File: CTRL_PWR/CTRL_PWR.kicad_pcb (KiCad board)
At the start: 2 copper layers, 34 x 17 mm, 9 parts, among them J1 BM09B-NSHSS-TBT_LF__SN_

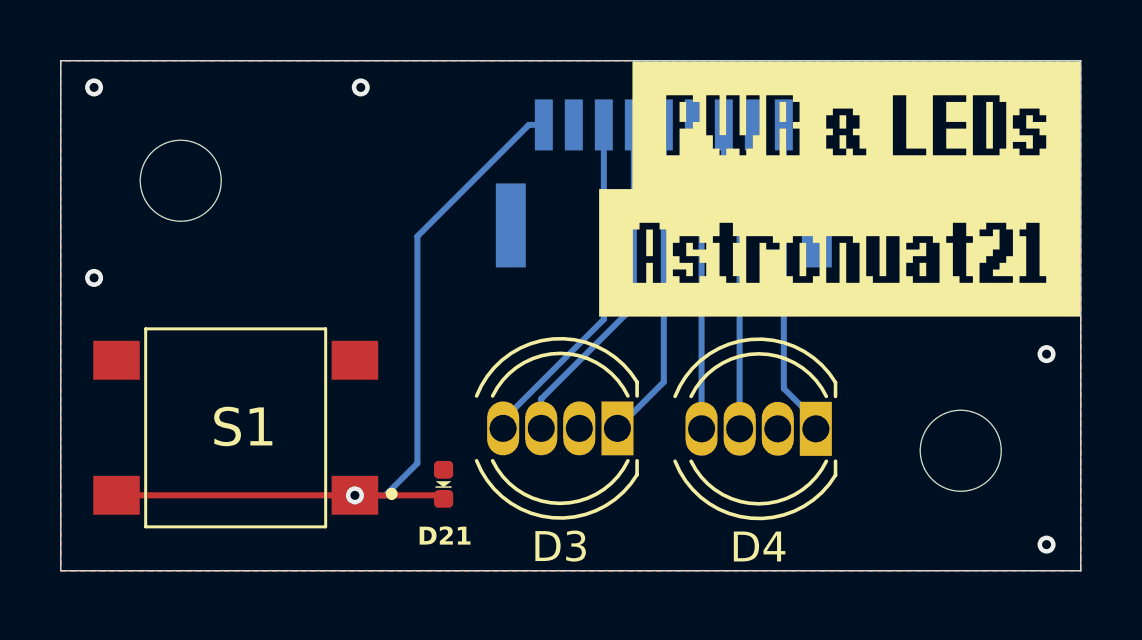
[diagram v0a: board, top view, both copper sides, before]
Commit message: CTRL_PWR updated to use 8P FPC Connector
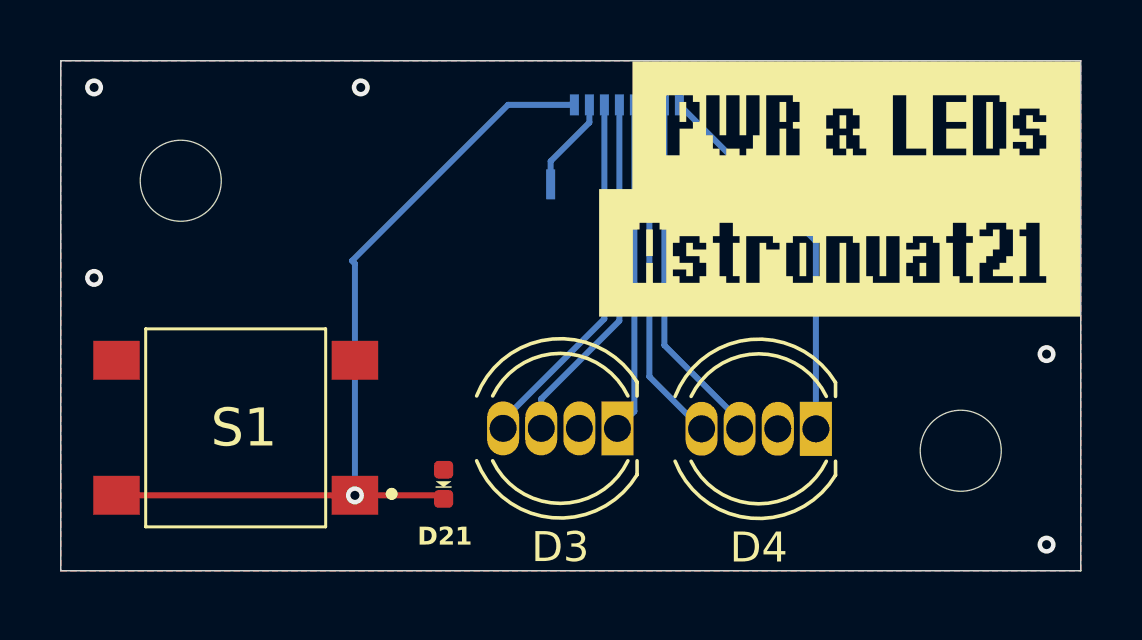
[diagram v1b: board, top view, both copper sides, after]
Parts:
- removed J1: BM09B-NSHSS-TBT_LF__SN_, BM09B-NSHSS-TBT_LF__SN_:BM09BNSHSSTBTLFSN
- added J2: 503480-0800, 503480-0800:5034800800, B.Cu at (94.0, 105.0)
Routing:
- net GND: track 0.00 -> 3.18 mm
- net Net-(D4-RA): track 10.6 -> 12.7 mm
- net Net-(D21-A1): track 26.8 -> 28.4 mm
- net Net-(D4-GA): track 10.3 -> 11.8 mm
- net Net-(D4-BA): track 10.4 -> 11.5 mm
- net Net-(D3-BA): track 11.5 -> 12.2 mm

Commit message: Updated CTRL_Z to use 3 pin FPC and ESD Protection.
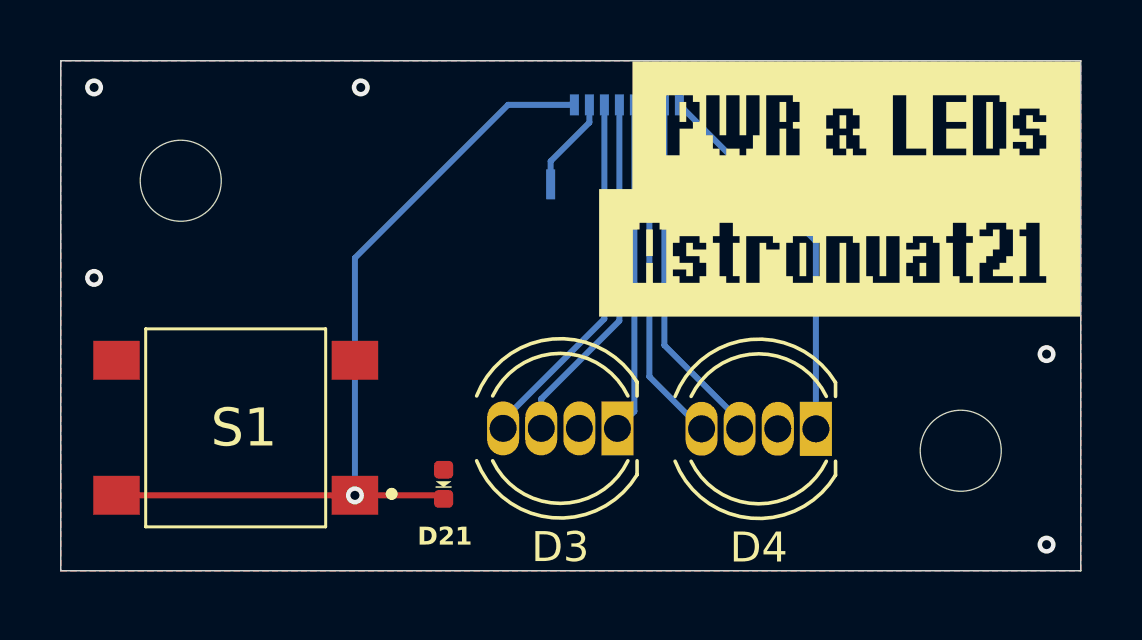
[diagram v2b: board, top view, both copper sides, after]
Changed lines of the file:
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@@
 	)
 	(segment
-		(start 84.8 108.65)
-		(end 84.895 108.745)
+		(start 92.21 103.45)
+		(end 90 103.45)
+		(width 0.2)
+		(layer "B.Cu")
+		(net "Net-(D21-A1)")
+	)
+	(segment
+		(start 84.895 108.555)
+		(end 84.895 116.468)
 		(width 0.2)
 		(layer "B.Cu")
@@
 	(segment
 		(start 90 103.45)
-		(end 84.8 108.65)
+		(end 84.895 108.555)
 		(width 0.2)
 		(layer "B.Cu")
-		(net "Net-(D21-A1)")
-	)
-	(segment
-		(start 84.895 108.745)
-		(end 84.895 116.468)
-		(width 0.2)
-		(layer "B.Cu")
-		(net "Net-(D21-A1)")
-	)
-	(segment
-		(start 92.21 103.45)
-		(end 90 103.45)
-		(width 0.2)
-		(layer "B.Cu")

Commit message: Added resistors to the LEDs on CTRL_PWR
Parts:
- removed kibuzzard-6A2CAA19: G***, kibuzzard-6A2CAA19
- added R1: 180R, Resistor_SMD:R_0402_1005Metric, B.Cu at (93.7, 110.0)
- added R2: 180R, Resistor_SMD:R_0402_1005Metric, B.Cu at (100.2, 110.0)
- added R3: 47R, Resistor_SMD:R_0402_1005Metric, B.Cu at (91.1, 109.9)
- added R4: 47R, Resistor_SMD:R_0402_1005Metric, B.Cu at (89.8, 110.0)
- added R5: 47R, Resistor_SMD:R_0402_1005Metric, B.Cu at (97.7, 109.9)
- added R6: 47R, Resistor_SMD:R_0402_1005Metric, B.Cu at (96.5, 110.0)
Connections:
- J2 pad 1: Net-(D4-RA) -> Net-(J2-Pad1)
- J2 pad 2: Net-(D4-GA) -> Net-(J2-Pad2)
- J2 pad 3: Net-(D4-BA) -> Net-(J2-Pad3)
- J2 pad 4: Net-(D3-RA) -> Net-(J2-Pad4)
- J2 pad 5: Net-(D3-GA) -> Net-(J2-Pad5)
- J2 pad 6: Net-(D3-BA) -> Net-(J2-Pad6)
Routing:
- net Net-(D4-RA): track 12.7 -> 3.79 mm
- net Net-(D3-BA): track 12.2 -> 3.74 mm
- net Net-(D3-GA): track 11.9 -> 3.79 mm
- net Net-(D4-GA): track 11.8 -> 3.81 mm
- net Net-(J2-Pad1): track 0.00 -> 7.87 mm
- net Net-(D4-BA): track 11.5 -> 3.79 mm
- net Net-(J2-Pad6): track 0.00 -> 7.42 mm
- net Net-(D3-RA): track 11.0 -> 3.80 mm
- net Net-(J2-Pad5): track 0.00 -> 7.06 mm
- net Net-(J2-Pad2): track 0.00 -> 7.01 mm
- net Net-(J2-Pad3): track 0.00 -> 6.71 mm
- net Net-(J2-Pad4): track 0.00 -> 6.20 mm

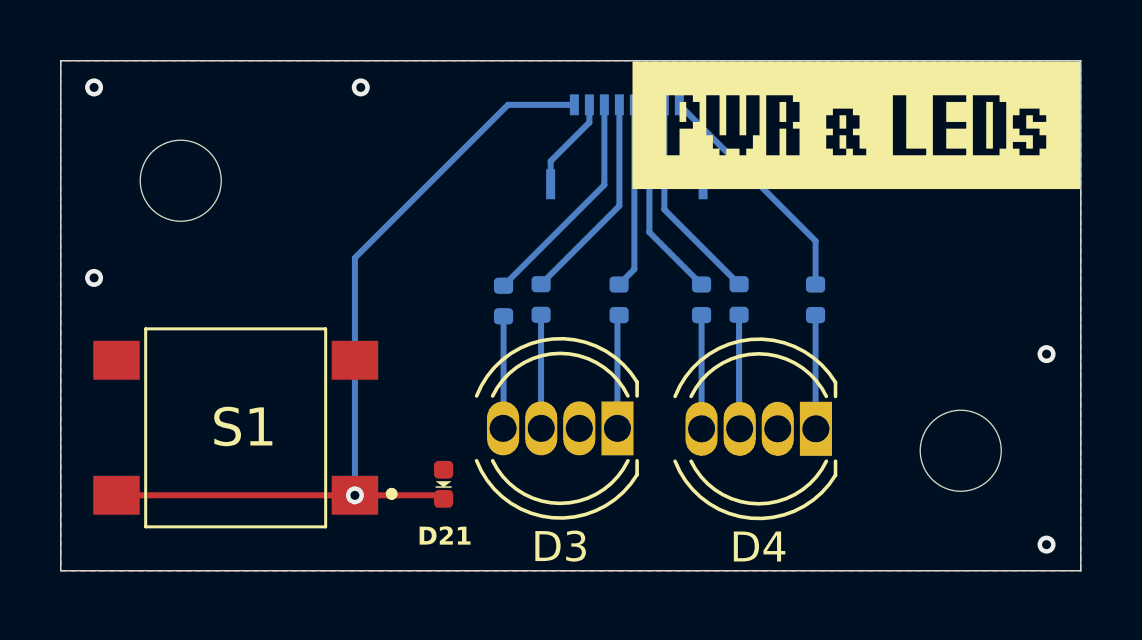
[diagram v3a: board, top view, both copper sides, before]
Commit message: Updated CTRLs to be one sided (saves a billion dollars somehow), added LCSC_Parts for BOM, and other fixes. (Part 1/2)
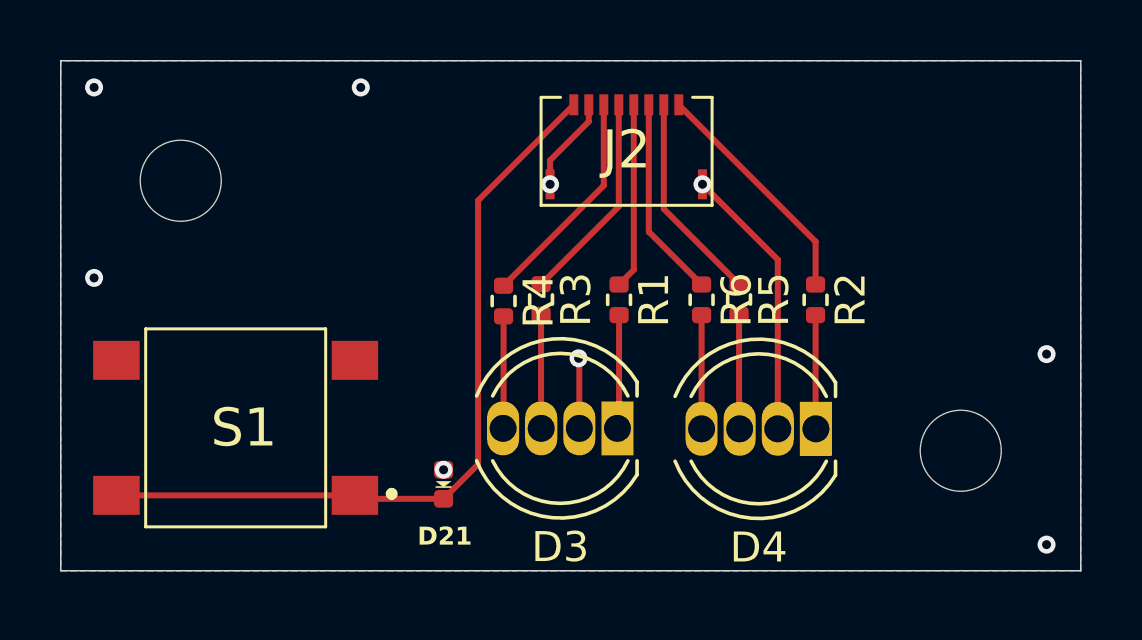
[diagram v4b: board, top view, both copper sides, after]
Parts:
- removed kibuzzard-6A2CA9F9: G***, kibuzzard-6A2CA9F9
- J2, R1, R2, R3, R4, R5, R6: moved to F.Cu
- turned J2 to 0 degrees
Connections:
- J2 pad 1: Net-(J2-Pad1) -> Net-(D21-A1)
- J2 pad 2: Net-(J2-Pad2) -> GND
- J2 pad 7: GND -> Net-(J2-Pad7)
- J2 pad 8: Net-(D21-A1) -> Net-(J2-Pad8)
- R1 pad 1: Net-(J2-Pad4) -> Net-(J2-Pad5)
- R2 pad 1: Net-(J2-Pad1) -> Net-(J2-Pad8)
- R3 pad 1: Net-(J2-Pad5) -> Net-(J2-Pad4)
- R4 pad 1: Net-(J2-Pad6) -> Net-(J2-Pad3)
- R5 pad 1: Net-(J2-Pad2) -> Net-(J2-Pad7)
- R6 pad 1: Net-(J2-Pad3) -> Net-(J2-Pad6)
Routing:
- net GND: track 3.18 -> 14.7 mm, vias 5 -> 9
- net Net-(J2-Pad8): track 0.00 -> 7.88 mm
- net Net-(J2-Pad1): track 7.87 -> 0.00 mm
- net Net-(J2-Pad7): track 0.00 -> 7.02 mm
- net Net-(J2-Pad2): track 7.01 -> 0.00 mm
- net Net-(D21-A1): track 28.3 -> 25.9 mm, vias 1 -> 0
- net Net-(J2-Pad5): track 7.06 -> 6.19 mm
- net Net-(J2-Pad4): track 6.20 -> 7.05 mm
- net Net-(J2-Pad3): track 6.71 -> 7.41 mm
- net Net-(J2-Pad6): track 7.42 -> 6.72 mm

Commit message: Completed routing of 9V and 3.3V of PSU
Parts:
- removed D21: ESD5V0B03, A_HDJ_Library:D_0402_1005Metric
- removed R1, R2: 180R, Resistor_SMD:R_0402_1005Metric
- removed R3, R4, R5, R6: 47R, Resistor_SMD:R_0402_1005Metric
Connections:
- J2 pad 3: Net-(J2-Pad3) -> Net-(D3-BA)
- J2 pad 4: Net-(J2-Pad4) -> Net-(D3-GA)
- J2 pad 5: Net-(J2-Pad5) -> Net-(D3-RA)
- J2 pad 6: Net-(J2-Pad6) -> Net-(D4-BA)
- J2 pad 7: Net-(J2-Pad7) -> Net-(D4-GA)
- J2 pad 8: Net-(J2-Pad8) -> Net-(D4-RA)
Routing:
- net Net-(D4-RA): track 3.79 -> 12.7 mm
- net Net-(D3-BA): track 3.74 -> 12.2 mm
- net Net-(D3-GA): track 3.79 -> 11.9 mm
- net Net-(D4-GA): track 3.81 -> 11.8 mm
- net Net-(J2-Pad8): track 7.88 -> 0.00 mm
- net Net-(D4-BA): track 3.79 -> 11.5 mm
- net Net-(J2-Pad3): track 7.41 -> 0.00 mm
- net Net-(D3-RA): track 3.80 -> 11.0 mm
- net Net-(J2-Pad4): track 7.05 -> 0.00 mm
- net Net-(J2-Pad7): track 7.02 -> 0.00 mm
- net Net-(J2-Pad6): track 6.72 -> 0.00 mm
- net Net-(J2-Pad5): track 6.19 -> 0.00 mm
- net GND: vias 9 -> 8

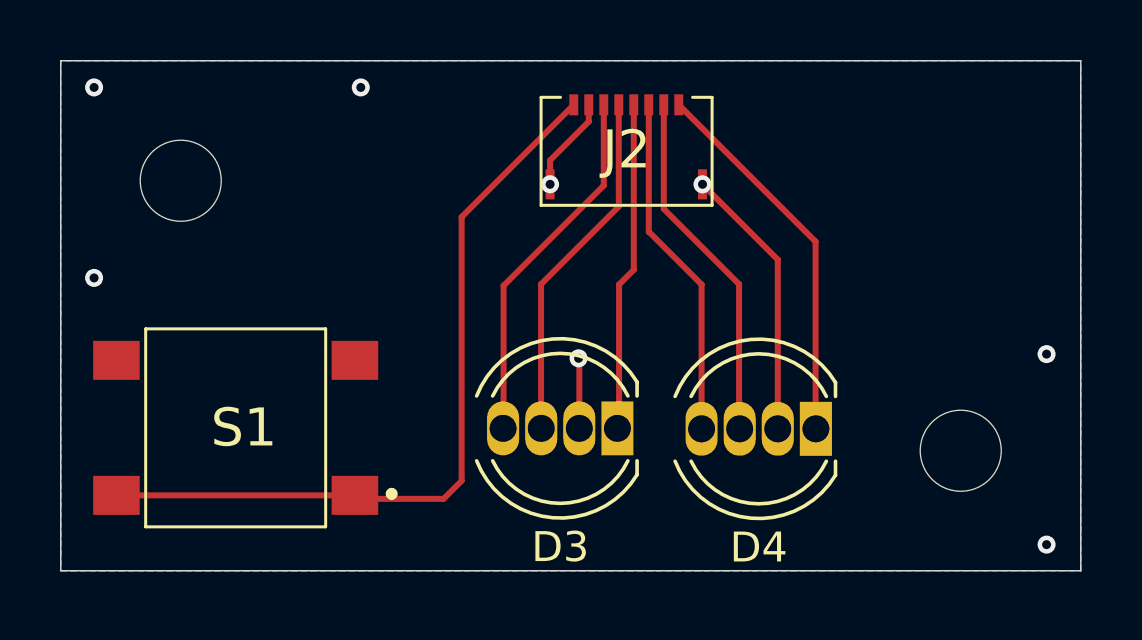
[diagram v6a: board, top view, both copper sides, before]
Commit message: Removed Vias-in-pads on all CTRL PCBs. (Saves Money!)
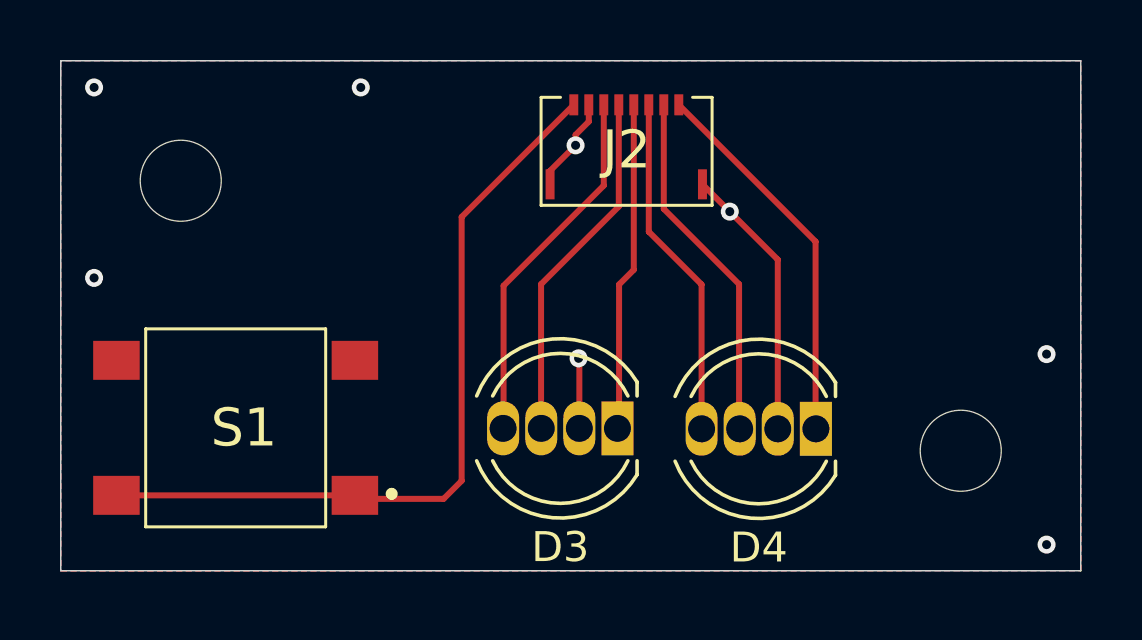
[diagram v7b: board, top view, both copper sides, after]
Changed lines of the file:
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@@
-	)
-	(segment
-		(start 98.99 108.61)
-		(end 98.99 114.25)
-		(width 0.2)
-		(layer "F.Cu")
-		(net "GND")
-	)
-	(segment
-		(start 91.4 105.3)
-		(end 91.4 106.1)
-		(width 0.2)
-		(layer "F.Cu")
-		(net "GND")
-	)
-	(segment
-		(start 96.48 106.1)
-		(end 98.99 108.61)
-		(width 0.2)
-		(layer "F.Cu")
-		(net "GND")
-	)
-	(segment
-		(start 92.69 104.01)
-		(end 91.4 105.3)
-		(width 0.2)
-		(layer "F.Cu")
-		(net "GND")
 	)
 	(segment
@@
 	)
 	(segment
-		(start 92.69 103.45)
-		(end 92.69 104.01)
+		(start 92.25 104.8)
+		(end 92.25 104.45)
+		(width 0.2)
+		(layer "F.Cu")
+		(net "GND")
+	)
+	(segment
+		(start 91.4 106.1)
+		(end 91.4 105.65)
+		(width 0.2)
+		(layer "F.Cu")
+		(net "GND")
+	)
+	(segment
+		(start 92.69 104.01)
+		(end 92.69 103.45)
+		(width 0.2)
+		(layer "F.Cu")
+		(net "GND")
+	)
+	(segment
+		(start 97.39 107.01)
+		(end 98.99 108.61)
 		(width 0.2)
 		(layer "F.Cu")
@@
 		(net "GND")
 	)
+	(segment
+		(start 91.4 105.65)
+		(end 92.25 104.8)
+		(width 0.2)
+		(layer "F.Cu")
+		(net "GND")
+	)
+	(segment
+		(start 98.99 108.61)
+		(end 98.99 114.25)
+		(width 0.2)
+		(layer "F.Cu")
+		(net "GND")
+	)
+	(segment
+		(start 92.25 104.45)
+		(end 92.69 104.01)
+		(width 0.2)
+		(layer "F.Cu")
+		(net "GND")
+	)
+	(segment
+		(start 96.48 106.1)
+		(end 97.39 107.01)
+		(width 0.2)
+		(layer "F.Cu")
+		(net "GND")
+	)
 	(via
-		(at 91.4 106.1)
+		(at 92.25 104.8)
 		(size 0.6)
 		(drill 0.3)
@@
 	)
 	(via
-		(at 96.48 106.1)
+		(at 97.39 107.01)
 		(size 0.6)
 		(drill 0.3)
